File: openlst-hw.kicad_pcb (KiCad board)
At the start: 4 copper layers, 80 x 80 mm, 152 parts, among them J1 CC Prog/Debug, J10 Conn_01x03_Pin, J11 Conn_01x03_Pin, J12 Conn_01x03_Pin, J13 10155435-00011LF, J2 UART0, J3 Control Outputs, J4 Control Outputs, J5 ANT, J6 Switch Select, J7 Conn_Coaxial, J8 PC104 Conn_02x20_Odd_Even, J9 Conn_01x05_Pin, SW1 EVP-AA602W, SW2 EVP-AA602W, U1 CC1110, U10 AP3602AKTR-G1, U11 STM32L496RGTx, U12 74LVC2G07, U2 MIC803, U3 SF2446E, U4 PE4250MLI, U5 PE4250MLI, U6 0433BM15A0001, U7 RFFM6406, U8 TJA1042TK-3, U9 TJA1042TK-3, X1 27MHz, X2 10MHz

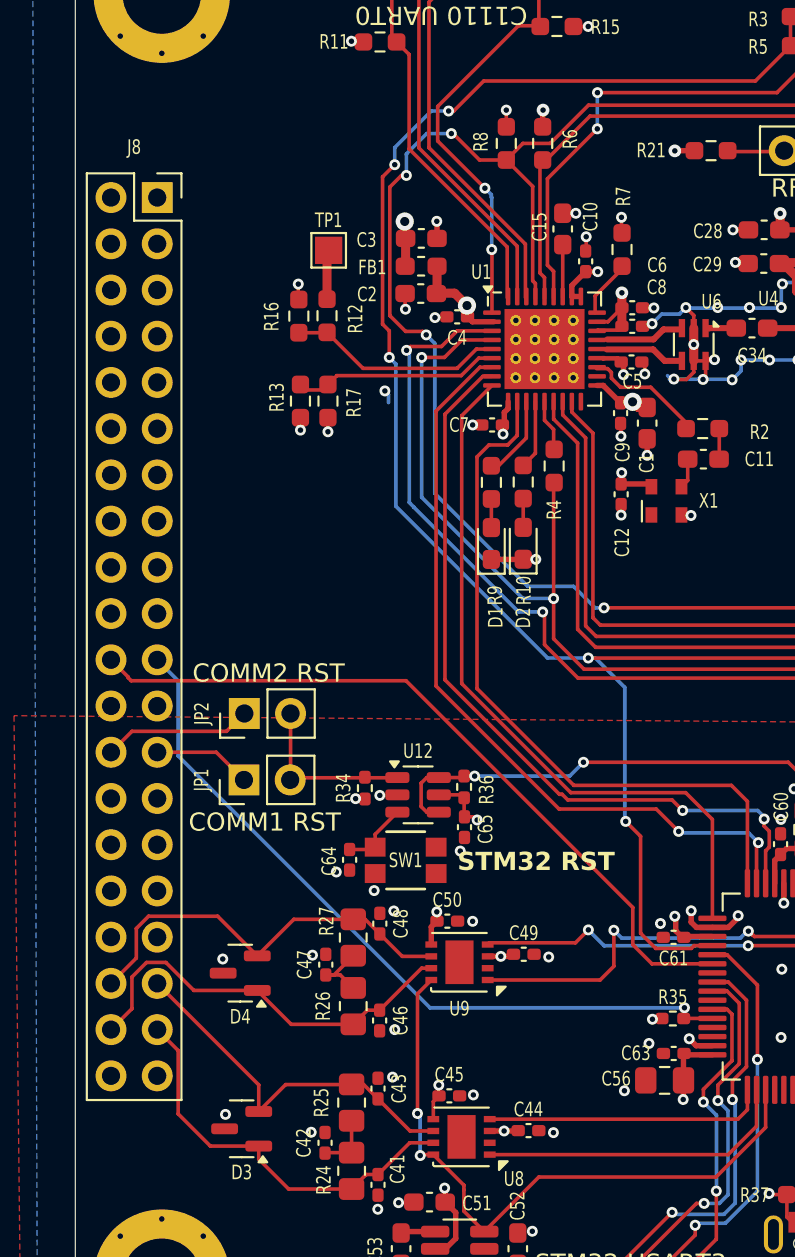
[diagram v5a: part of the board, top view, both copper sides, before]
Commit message: openlst board to updated pc104 layout
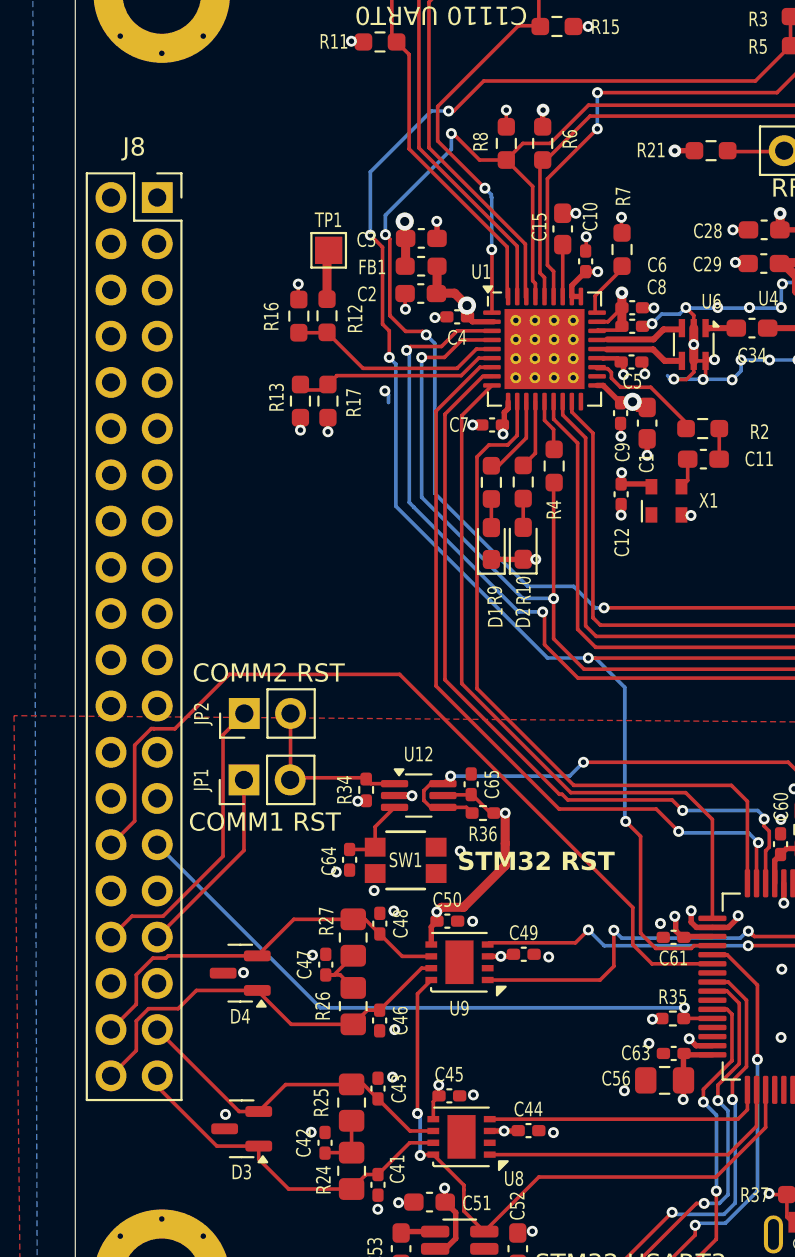
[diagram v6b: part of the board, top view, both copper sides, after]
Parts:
- U12: footprint Package_TO_SOT_SMD:SOT-23-6 -> Package_TO_SOT_SMD:SOT-363_SC-70-6_Handsoldering
- moved C65 2.38 mm to (81.8, 108.1), turned to -90 degrees
- moved R36 1.77 mm to (82.4, 109.7), turned to 180 degrees
- moved R34 0.12 mm to (76.0, 108.5)
- moved U12 0.05 mm to (78.9, 108.8)
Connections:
- net /CAN Bridge/PMIC/Schmitt Trigger/IN1 renamed /CAN Bridge/PMIC/Schmitt Trigger/IN2
- net /INTERBOARD_CONNECTOR2/3V3_1 renamed /INTERBOARD_CONNECTOR2/3V3_15_EXTRA2
- net /INTERBOARD_CONNECTOR2/3V3_13 renamed /INTERBOARD_CONNECTOR2/3V3_1_AVI_STM_CORE
- net /INTERBOARD_CONNECTOR2/3V3_2 renamed /INTERBOARD_CONNECTOR2/3V3_4_AVI_SUN
- net /INTERBOARD_CONNECTOR2/3V3_3 renamed /INTERBOARD_CONNECTOR2/3V3_5_AVI_ACS_LOGIC
- net /INTERBOARD_CONNECTOR2/3V3_4 renamed /INTERBOARD_CONNECTOR2/3V3_8_AVI_CLK
- net /INTERBOARD_CONNECTOR2/3V3_5 renamed /INTERBOARD_CONNECTOR2/3V3_9_SCI_STM_CORE
- net /INTERBOARD_CONNECTOR2/3V3_6 renamed /INTERBOARD_CONNECTOR2/3V3_10_SCI_MRAM
- net /INTERBOARD_CONNECTOR2/3V3_7 renamed /INTERBOARD_CONNECTOR2/3V3_11_SCI_FLASH
- net /INTERBOARD_CONNECTOR2/3V3_8 renamed /INTERBOARD_CONNECTOR2/3V3_6_AVI_GYRO
- net /INTERBOARD_CONNECTOR2/3V3_9 renamed /INTERBOARD_CONNECTOR2/3V3_7_AVI_MAG
- C12 pad 1: /3V3_COMM -> /INTERBOARD_CONNECTOR2/3V3_18_RF1_COMM
- C13 pad 2: /3V3_COMM -> /INTERBOARD_CONNECTOR2/3V3_18_RF1_COMM
- C16 pad 1: /3V3_COMM -> /INTERBOARD_CONNECTOR2/3V3_18_RF1_COMM
- C18 pad 1: /VRF -> /INTERBOARD_CONNECTOR2/BATT_1_COMM1_VRF
- C19 pad 1: /VRF -> /INTERBOARD_CONNECTOR2/BATT_1_COMM1_VRF
- C20 pad 1: /VRF -> /INTERBOARD_CONNECTOR2/BATT_1_COMM1_VRF
- C21 pad 1: /VRF -> /INTERBOARD_CONNECTOR2/BATT_1_COMM1_VRF
- C22 pad 1: /VRF -> /INTERBOARD_CONNECTOR2/BATT_1_COMM1_VRF
- C23 pad 1: /VRF -> /INTERBOARD_CONNECTOR2/BATT_1_COMM1_VRF
- C25 pad 1: /VRF -> /INTERBOARD_CONNECTOR2/BATT_1_COMM1_VRF
- C26 pad 1: /VRF -> /INTERBOARD_CONNECTOR2/BATT_1_COMM1_VRF
- C27 pad 1: /VRF -> /INTERBOARD_CONNECTOR2/BATT_1_COMM1_VRF
- C28 pad 1: /3V3_COMM -> /INTERBOARD_CONNECTOR2/3V3_18_RF1_COMM
- C3 pad 1: /3V3_COMM -> /INTERBOARD_CONNECTOR2/3V3_18_RF1_COMM
- C30 pad 1: /3V3_COMM -> /INTERBOARD_CONNECTOR2/3V3_18_RF1_COMM
- C38 pad 1: /3V3_COMM -> /INTERBOARD_CONNECTOR2/3V3_18_RF1_COMM
- C39 pad 1: /3V3_COMM -> /INTERBOARD_CONNECTOR2/3V3_18_RF1_COMM
- C40 pad 1: /3V3_BRIDGE -> /INTERBOARD_CONNECTOR2/3V3_17_RF1_BRIDGE
- C45 pad 1: /3V3_CAN -> /INTERBOARD_CONNECTOR2/3V3_17_RF1_BRIDGE
- C50 pad 1: /3V3_CAN -> /INTERBOARD_CONNECTOR2/3V3_17_RF1_BRIDGE
- C51 pad 1: /3V3_CAN -> /INTERBOARD_CONNECTOR2/3V3_17_RF1_BRIDGE
- C54 pad 1: /3V3_BRIDGE -> /INTERBOARD_CONNECTOR2/3V3_17_RF1_BRIDGE
- C55 pad 1: /3V3_BRIDGE -> /INTERBOARD_CONNECTOR2/3V3_17_RF1_BRIDGE
- C56 pad 1: /3V3_BRIDGE -> /INTERBOARD_CONNECTOR2/3V3_17_RF1_BRIDGE
- C57 pad 1: /3V3_BRIDGE -> /INTERBOARD_CONNECTOR2/3V3_17_RF1_BRIDGE
- C58 pad 1: /3V3_BRIDGE -> /INTERBOARD_CONNECTOR2/3V3_17_RF1_BRIDGE
- C59 pad 1: /3V3_BRIDGE -> /INTERBOARD_CONNECTOR2/3V3_17_RF1_BRIDGE
- C60 pad 1: /3V3_BRIDGE -> /INTERBOARD_CONNECTOR2/3V3_17_RF1_BRIDGE
- C61 pad 1: /3V3_BRIDGE -> /INTERBOARD_CONNECTOR2/3V3_17_RF1_BRIDGE
- C62 pad 1: /3V3_BRIDGE -> /INTERBOARD_CONNECTOR2/3V3_17_RF1_BRIDGE
- C63 pad 1: /3V3_BRIDGE -> /INTERBOARD_CONNECTOR2/3V3_17_RF1_BRIDGE
- C65 pad 2: /3V3_BRIDGE -> /INTERBOARD_CONNECTOR2/3V3_17_RF1_BRIDGE
- FB1 pad 1: /3V3_COMM -> /INTERBOARD_CONNECTOR2/3V3_18_RF1_COMM
- FB2 pad 2: /3V3_COMM -> /INTERBOARD_CONNECTOR2/3V3_18_RF1_COMM
- FB3 pad 2: /3V3_COMM -> /INTERBOARD_CONNECTOR2/3V3_18_RF1_COMM
- FB4 pad 2: /3V3_COMM -> /INTERBOARD_CONNECTOR2/3V3_18_RF1_COMM
- J1 pad 2: /3V3_COMM -> /INTERBOARD_CONNECTOR2/3V3_18_RF1_COMM
- J2 pad 6: /3V3_COMM -> /INTERBOARD_CONNECTOR2/3V3_18_RF1_COMM
- J3 pad 3: /3V3_COMM -> /INTERBOARD_CONNECTOR2/3V3_18_RF1_COMM
- J4 pad 3: /3V3_COMM -> /INTERBOARD_CONNECTOR2/3V3_18_RF1_COMM
- J8 pad 10: /3V3_COMM -> /INTERBOARD_CONNECTOR2/3V3_14_EXTRA1
- J8 pad 11: /3V3_BRIDGE -> /INTERBOARD_CONNECTOR2/3V3_13_SCI_CAMERAS
- J8 pad 12: /3V3_CAN -> /INTERBOARD_CONNECTOR2/3V3_12_SCI_THERMAL
- J8 pad 21: /CAN Bridge/ATTENTION -> /INTERBOARD_CONNECTOR2/3V3_3_AVI_MRAM
- J8 pad 22: /CAN Bridge/EPS_RST -> /INTERBOARD_CONNECTOR2/3V3_2_AVI_GPS
- J8 pad 23: /INTERBOARD_CONNECTOR2/*SCI_RST -> /INTERBOARD_CONNECTOR2/3V3_17_RF1_BRIDGE
- J8 pad 24: /INTERBOARD_CONNECTOR2/*AVI_RST -> /INTERBOARD_CONNECTOR2/3V3_18_RF1_COMM
- J8 pad 25: /CAN Bridge/COMM1_RST -> /INTERBOARD_CONNECTOR2/3V3_19_RF2_BRIDGE
- J8 pad 26: /CAN Bridge/COMM2_RST -> /INTERBOARD_CONNECTOR2/3V3_20_RF2_COMM
- J8 pad 29: /INTERBOARD_CONNECTOR2/5V0_1 -> /CAN Bridge/ATTENTION
- J8 pad 3: /INTERBOARD_CONNECTOR2/BATT_1 -> /INTERBOARD_CONNECTOR2/BATT_1_COMM1_VRF
- J8 pad 30: /INTERBOARD_CONNECTOR2/5V0_2 -> /CAN Bridge/EPS_RST
- J8 pad 31: /INTERBOARD_CONNECTOR2/5V0_3 -> /INTERBOARD_CONNECTOR2/*SCI_RST
- J8 pad 32: /INTERBOARD_CONNECTOR2/5V0_4 -> /INTERBOARD_CONNECTOR2/*AVI_RST
- J8 pad 33: GND -> /CAN Bridge/COMM1_RST
- J8 pad 34: GND -> /CAN Bridge/COMM2_RST
- J8 pad 35: /CAN Bridge/CAN2_L -> GND
- J8 pad 36: /CAN Bridge/CAN1_L -> GND
- J8 pad 37: /CAN Bridge/CAN2_H -> /CAN Bridge/CAN2_L
- J8 pad 38: /CAN Bridge/CAN1_H -> /CAN Bridge/CAN1_L
- J8 pad 39: GND -> /CAN Bridge/CAN2_H
- J8 pad 4: /VRF -> /INTERBOARD_CONNECTOR2/BATT_2_COMM2_VRF
- J8 pad 40: GND -> /CAN Bridge/CAN1_H
- J8 pad 5: GND -> /INTERBOARD_CONNECTOR2/BATT_3_AVI_ACS_COIL
- J8 pad 6: GND -> /INTERBOARD_CONNECTOR2/BATT_4_SCI_CAMERAS
- R13 pad 2: /VRF -> /INTERBOARD_CONNECTOR2/BATT_1_COMM1_VRF
- R21 pad 1: /3V3_COMM -> /INTERBOARD_CONNECTOR2/3V3_18_RF1_COMM
- R22 pad 2: /3V3_COMM -> /INTERBOARD_CONNECTOR2/3V3_18_RF1_COMM
- R3 pad 2: /3V3_COMM -> /INTERBOARD_CONNECTOR2/3V3_18_RF1_COMM
- R34 pad 1: /3V3_BRIDGE -> /INTERBOARD_CONNECTOR2/3V3_17_RF1_BRIDGE
- R35 pad 1: /3V3_BRIDGE -> /INTERBOARD_CONNECTOR2/3V3_17_RF1_BRIDGE
- R36 pad 1: /3V3_BRIDGE -> /INTERBOARD_CONNECTOR2/3V3_17_RF1_BRIDGE
- R6 pad 2: /3V3_COMM -> /INTERBOARD_CONNECTOR2/3V3_18_RF1_COMM
- SW2 pad 3: /3V3_BRIDGE -> /INTERBOARD_CONNECTOR2/3V3_17_RF1_BRIDGE
- U10 pad 5: /3V3_CAN -> /INTERBOARD_CONNECTOR2/3V3_17_RF1_BRIDGE
- U11 pad 1: /3V3_BRIDGE -> /INTERBOARD_CONNECTOR2/3V3_17_RF1_BRIDGE
- U11 pad 13: /3V3_BRIDGE -> /INTERBOARD_CONNECTOR2/3V3_17_RF1_BRIDGE
- U11 pad 19: /3V3_BRIDGE -> /INTERBOARD_CONNECTOR2/3V3_17_RF1_BRIDGE
- U11 pad 32: /3V3_BRIDGE -> /INTERBOARD_CONNECTOR2/3V3_17_RF1_BRIDGE
- U11 pad 48: /3V3_BRIDGE -> /INTERBOARD_CONNECTOR2/3V3_17_RF1_BRIDGE
- U11 pad 64: /3V3_BRIDGE -> /INTERBOARD_CONNECTOR2/3V3_17_RF1_BRIDGE
- U12 pad 5: /3V3_BRIDGE -> /INTERBOARD_CONNECTOR2/3V3_17_RF1_BRIDGE
- U2 pad 3: /3V3_COMM -> /INTERBOARD_CONNECTOR2/3V3_18_RF1_COMM
- U7 pad 17: /VRF -> /INTERBOARD_CONNECTOR2/BATT_1_COMM1_VRF
- U7 pad 23: /3V3_COMM -> /INTERBOARD_CONNECTOR2/3V3_18_RF1_COMM
- U7 pad 24: /VRF -> /INTERBOARD_CONNECTOR2/BATT_1_COMM1_VRF
- U7 pad 26: /VRF -> /INTERBOARD_CONNECTOR2/BATT_1_COMM1_VRF
- U8 pad 5: /3V3_CAN -> /INTERBOARD_CONNECTOR2/3V3_17_RF1_BRIDGE
- U9 pad 5: /3V3_CAN -> /INTERBOARD_CONNECTOR2/3V3_17_RF1_BRIDGE
- X1 pad 4: /3V3_COMM -> /INTERBOARD_CONNECTOR2/3V3_18_RF1_COMM
- X2 pad 1: /3V3_BRIDGE -> /INTERBOARD_CONNECTOR2/3V3_17_RF1_BRIDGE
- X2 pad 4: /3V3_BRIDGE -> /INTERBOARD_CONNECTOR2/3V3_17_RF1_BRIDGE
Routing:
- net /INTERBOARD_CONNECTOR2/BATT_1_COMM1_VRF: track 0.00 -> 130.3 mm, vias 0 -> 4
- net /VRF: track 130.0 -> 0.00 mm, vias 4 -> 0
- net /INTERBOARD_CONNECTOR2/3V3_17_RF1_BRIDGE: track 0.00 -> 87.7 mm, vias 0 -> 14
- net /3V3_BRIDGE: track 84.3 -> 0.00 mm, vias 11 -> 0
- net /3V3_CAN: track 64.9 -> 0.00 mm, vias 3 -> 0
- net /INTERBOARD_CONNECTOR2/3V3_18_RF1_COMM: track 0.00 -> 61.0 mm, vias 0 -> 12
- net /3V3_COMM: track 61.0 -> 0.00 mm, vias 12 -> 0
- net /CAN Bridge/COMM2_RST: track 8.21 -> 16.3 mm
- net /CAN Bridge/ATTENTION: track 41.5 -> 34.9 mm
- net /CAN Bridge/EPS_RST: track 41.2 -> 47.2 mm
- net /CAN Bridge/COMM1_RST: track 5.39 -> 10.6 mm
- net /CAN Bridge/CAN2_H: track 22.3 -> 19.6 mm
- net /CAN Bridge/CAN2_L: track 20.6 -> 18.7 mm
- net /CAN Bridge/PMIC/Schmitt Trigger/OUT: track 30.6 -> 31.8 mm
- net /CAN Bridge/CAN1_L: track 22.7 -> 21.9 mm
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- added copper zone on In2.Cu, net /INTERBOARD_CONNECTOR2/3V3_17_RF1_BRIDGE
- added copper zone on In2.Cu, net /INTERBOARD_CONNECTOR2/3V3_18_RF1_COMM
- added copper zone on In2.Cu, net /INTERBOARD_CONNECTOR2/BATT_1_COMM1_VRF
- removed copper zone on In2.Cu, net /3V3_BRIDGE
- removed copper zone on In2.Cu, net /3V3_CAN
- removed copper zone on In2.Cu, net /3V3_COMM
- removed copper zone on In2.Cu, net /VRF
